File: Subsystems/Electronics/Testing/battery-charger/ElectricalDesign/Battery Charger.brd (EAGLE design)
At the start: 165 x 75 mm, 140 parts, among them J1 USB4515-GF-A_REVA, J3 10103592-0001LF, Q1 CSD16406Q3, Q2 CSD16406Q3, Q3 DMN2008LFU, Q4 DMN2008LFU, Q5 DMN2008LFU, Q6 BC817, Q7 BC817, Q8 DMN53D0L, SW6 [Override], U1 BQ24650, U2 BQ29700, U3 BQ29700, U4 BQ29700, U5 CP2102N-A02-GQFN28, U7 ESP32-S2-MINI-1

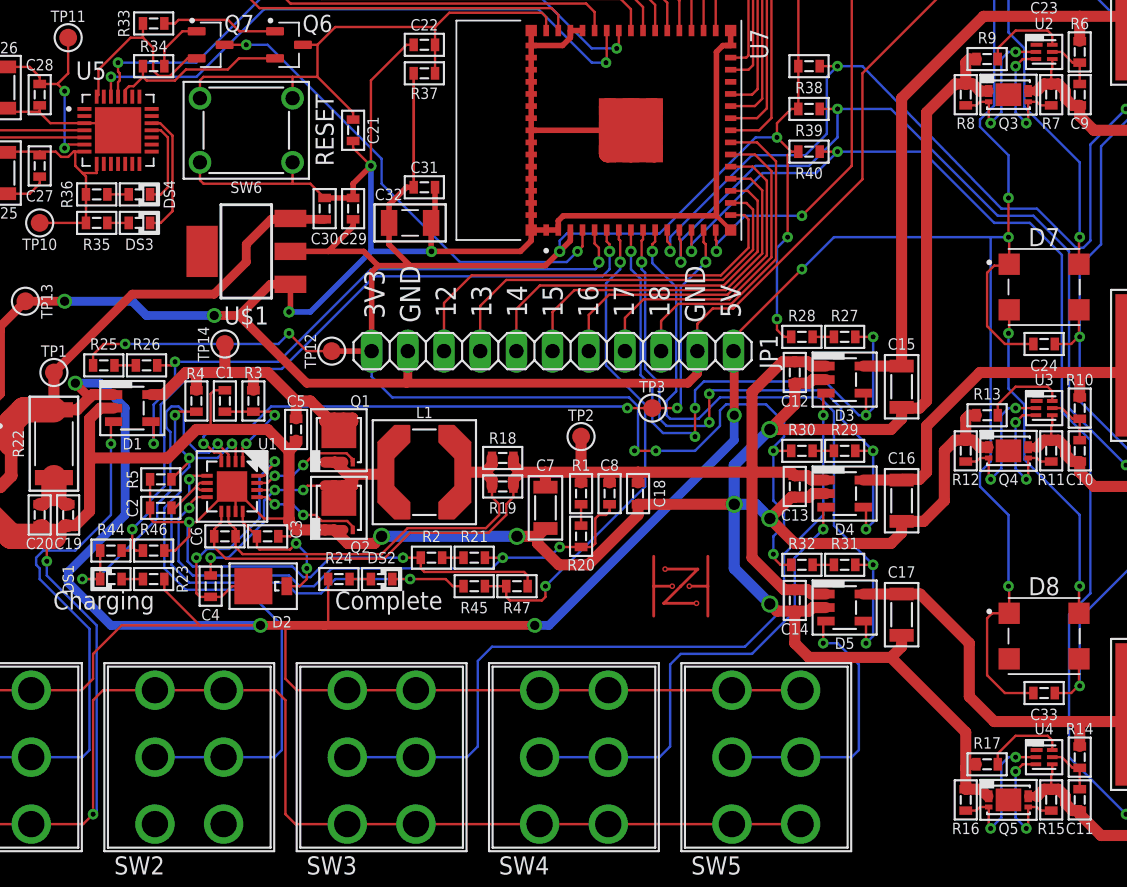
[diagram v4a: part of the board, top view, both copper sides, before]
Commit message: Removed Wire Stubs
Ran DRC a dozen times and cleaned up all the errors and wire stubs
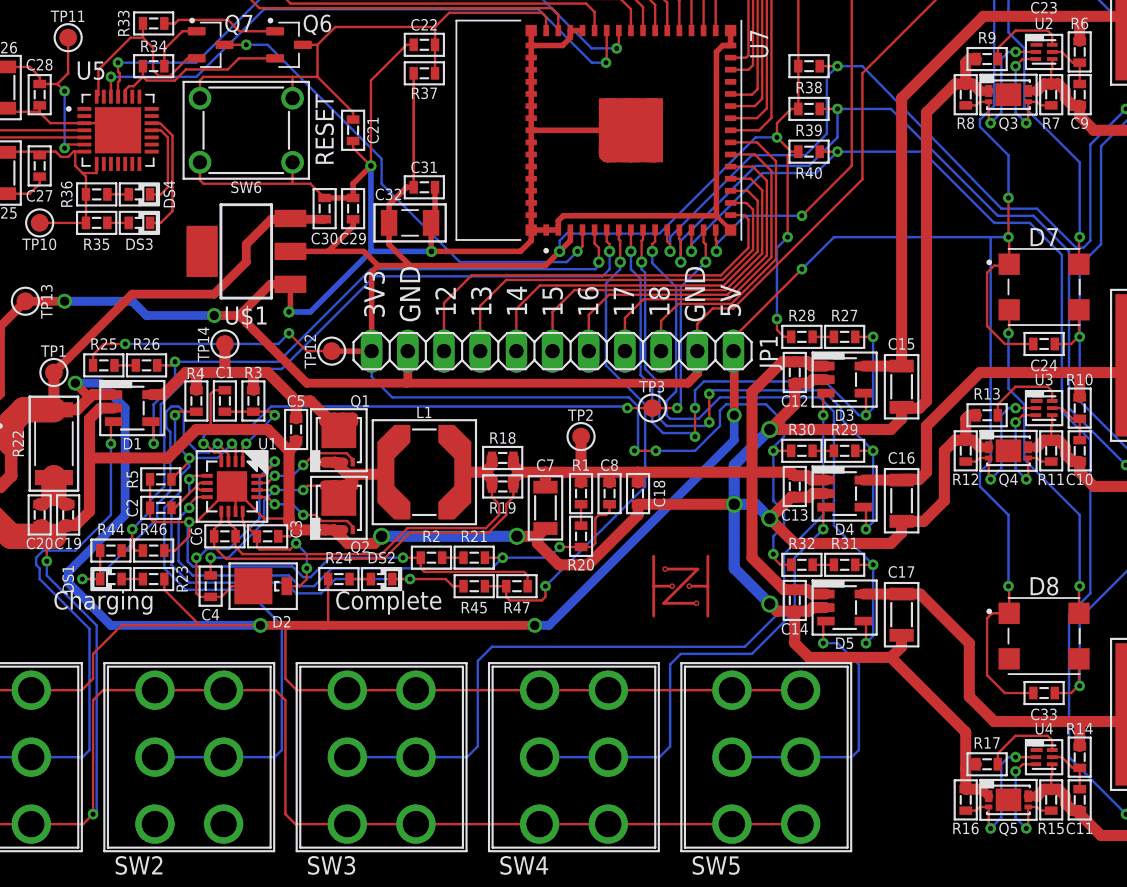
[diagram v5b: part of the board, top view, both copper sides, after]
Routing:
- net PGND: track 781.8 -> 779.6 mm
- net BQ24650_PH: track 23.8 -> 23.1 mm
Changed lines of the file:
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@@
 <wire x1="32.125" y1="26" x2="34" y2="26" width="0.78" layer="1"/>
 <wire x1="44" y1="26.5" x2="45.45" y2="26.5" width="0.78" layer="1"/>
-<wire x1="45.45" y1="26.5" x2="46" y2="27.05" width="0.78" layer="1"/>
 <wire x1="34.5" y1="26.5" x2="44" y2="26.5" width="0.78" layer="16"/>
-<wire x1="45.45" y1="26.3" x2="45.45" y2="26.5" width="0.17" layer="1"/>
 <wire x1="28.1" y1="26.5" x2="28.55" y2="26.95" width="0.17" layer="1"/>
 <wire x1="27.25" y1="26.5" x2="28.1" y2="26.5" width="0.17" layer="1"/>
 <wire x1="24" y1="30" x2="21.5" y2="27.5" width="0.17" layer="1"/>
-<wire x1="23.5" y1="36.75" x2="23.75" y2="36.75" width="0.17" layer="1"/>
 <wire x1="18.5" y1="27.5" x2="18.25" y2="27.75" width="0.17" layer="1"/>
 <wire x1="18.25" y1="27.75" x2="18.25" y2="28.5" width="0.17" layer="1"/>
@@
 <wire x1="14.75" y1="35.5" x2="14" y2="34.75" width="0.78" layer="1"/>
 <wire x1="14" y1="34.75" x2="14" y2="32" width="0.78" layer="1"/>
-<wire x1="23.5" y1="36.75" x2="22.75" y2="36.75" width="0.17" layer="1"/>
-<wire x1="22.75" y1="36.75" x2="22.5" y2="36.5" width="0.17" layer="1"/>
+<wire x1="22.5" y1="36.5" x2="22.75" y2="36.75" width="0.17" layer="1"/>
 <wire x1="22.5" y1="36.5" x2="22.5" y2="34" width="0.17" layer="1"/>
 <wire x1="52.5" y1="28.75" x2="52.5" y2="28" width="0.78" layer="1"/>
 <wire x1="46.94806875" y1="24.5" x2="45.45" y2="25.99806875" width="0.78" layer="1"/>
-<wire x1="45.45" y1="25.99806875" x2="45.45" y2="26.5" width="0.78" layer="1"/>
 <wire x1="52.5" y1="28" x2="49" y2="24.5" width="0.78" layer="1"/>
 <wire x1="49" y1="24.5" x2="46.94806875" y2="24.5" width="0.78" layer="1"/>
@@
 <wire x1="75.5" y1="58.25" x2="76" y2="58.25" width="0.78" layer="1"/>
 <wire x1="76" y1="58.25" x2="76.5" y2="57.75" width="0.78" layer="1"/>
-<wire x1="77.0526" y1="57.75" x2="76.5" y2="57.75" width="0.78" layer="1"/>
-<wire x1="77.0526" y1="57.75" x2="77.0576" y2="57.755" width="0.78" layer="1"/>
 <wire x1="71" y1="27.55" x2="72.55" y2="27.55" width="0.78" layer="1"/>
 <wire x1="74" y1="29" x2="72.55" y2="27.55" width="0.78" layer="1"/>
@@
 <wire x1="75.5" y1="33.25" x2="76" y2="33.25" width="0.78" layer="1"/>
 <wire x1="76" y1="33.25" x2="76.5" y2="32.75" width="0.78" layer="1"/>
-<wire x1="77.0526" y1="32.75" x2="76.5" y2="32.75" width="0.78" layer="1"/>
-<wire x1="77.0526" y1="32.75" x2="77.0576" y2="32.755" width="0.78" layer="1"/>
 <wire x1="75.5" y1="8.75" x2="75.5" y2="10.25" width="0.78" layer="1"/>
 <wire x1="75.5" y1="10.25" x2="75.75" y2="10.5" width="0.78" layer="1"/>
@@
 <wire x1="75.5" y1="12.75" x2="70.25" y2="18" width="0.78" layer="1"/>
 <wire x1="75.5" y1="8.75" x2="76.5626" y2="8.75" width="0.78" layer="1"/>
-<wire x1="76.5626" y1="8.75" x2="77.0576" y2="8.255" width="0.78" layer="1"/>
 <wire x1="83.45" y1="65.55" x2="83.5" y2="65.5" width="0.17" layer="1"/>
 <wire x1="83.45" y1="67.4" x2="83.45" y2="65.55" width="0.17" layer="1"/>
@@
 <wire x1="87.5" y1="24.75" x2="87.5" y2="32" width="0.17" layer="16"/>
 <wire x1="31.175" y1="26.95" x2="30.525" y2="26.95" width="0.78" layer="1"/>
-<wire x1="76.5" y1="57.75" x2="76.505" y2="57.755" width="0.16" layer="1"/>
-<wire x1="76.505" y1="57.755" x2="77.115" y2="57.755" width="0.16" layer="1"/>
-<wire x1="76.5" y1="32.75" x2="76.505" y2="32.755" width="0.16" layer="1"/>
-<wire x1="76.505" y1="32.755" x2="77.115" y2="32.755" width="0.16" layer="1"/>
-<wire x1="76.5626" y1="8.75" x2="76.62" y2="8.75" width="0.16" layer="1"/>
-<wire x1="76.62" y1="8.75" x2="77.115" y2="8.255" width="0.16" layer="1"/>
+<wire x1="76.62" y1="8.75" x2="76.5626" y2="8.75" width="0.16" layer="1"/>
 <wire x1="28.55" y1="26.95" x2="30.525" y2="26.95" width="0.78" layer="1"/>
 <contactref element="R47" pad="1"/>
@@
 <wire x1="20" y1="25.5" x2="21" y2="26.5" width="0.17" layer="1"/>
 <wire x1="21" y1="26.5" x2="21" y2="27.5" width="0.17" layer="1"/>
-<wire x1="31.825" y1="26.95" x2="31.175" y2="26.95" width="0.7" layer="1"/>
+<wire x1="31.825" y1="26.95" x2="31.175" y2="26.95" width="0.69" layer="1"/>
+<wire x1="77.115" y1="8.255" x2="76.62" y2="8.75" width="0.65" layer="1"/>
+<wire x1="45.45" y1="25.99806875" x2="45.45" y2="26.5" width="0.78" layer="1"/>
+<wire x1="45.45" y1="26.5" x2="46" y2="27.05" width="0.78" layer="1"/>
+<wire x1="22.75" y1="36.75" x2="23.5" y2="36.75" width="0.17" layer="1"/>
+<wire x1="76.5" y1="57.75" x2="77.11" y2="57.75" width="0.65" layer="1"/>
+<wire x1="77.11" y1="57.75" x2="77.115" y2="57.755" width="0.65" layer="1"/>
+<wire x1="76.5" y1="32.75" x2="77.11" y2="32.75" width="0.65" layer="1"/>
+<wire x1="77.11" y1="32.75" x2="77.115" y2="32.755" width="0.65" layer="1"/>
 </signal>
 <signal name="BQ24650_VREF">
@@
 <contactref element="Q2" pad="7"/>
 <contactref element="Q2" pad="5"/>
-<wire x1="30.475" y1="30" x2="30.525" y2="30.05" width="0.17" layer="1"/>
 <wire x1="34.6576" y1="30.8576" x2="34.8" y2="31" width="0.78" layer="1"/>
 <wire x1="32.10033125" y1="30.8576" x2="34.6576" y2="30.8576" width="0.78" layer="1"/>
@@
 <wire x1="25.75" y1="29.75" x2="27" y2="29.75" width="0.17" layer="1"/>
 <wire x1="29" y1="29.75" x2="29.3" y2="30.05" width="0.17" layer="1"/>
-<wire x1="29.3" y1="30.05" x2="30.525" y2="30.05" width="0.17" layer="1"/>
 <wire x1="27" y1="29.75" x2="29" y2="29.75" width="0.17" layer="16"/>
 <via x="22.5" y="25" extent="1-16" drill="0.35"/>
@@
 <wire x1="32.10033125" y1="30.8576" x2="32.475" y2="30.48293125" width="0.78" layer="1"/>
 <wire x1="30.525" y1="31.7" x2="31.175" y2="31.7" width="0.78" layer="1"/>
-<wire x1="31.175" y1="31.7" x2="31.7826" y2="31.7" width="0.78" layer="1"/>
 <wire x1="31.175" y1="31.7" x2="31.25793125" y2="31.7" width="0.78" layer="1"/>
 <wire x1="31.25793125" y1="31.7" x2="32.10033125" y2="30.8576" width="0.78" layer="1"/>
-<wire x1="31.175" y1="31.7" x2="31.825" y2="31.7" width="0.16" layer="1"/>
+<wire x1="31.825" y1="31.7" x2="31.175" y2="31.7" width="0.69" layer="1"/>
+<wire x1="29.3" y1="30.05" x2="30.525" y2="30.05" width="0.17" layer="1"/>
 </signal>
 <signal name="BQ24650_BTST">
@@
 <wire x1="80.495" y1="8.255" x2="80.5" y2="8.25" width="0.78" layer="1"/>
 <wire x1="80.5" y1="8.25" x2="81" y2="8.75" width="0.78" layer="1"/>
-<wire x1="79.885" y1="8.255" x2="80.495" y2="8.255" width="0.6" layer="1"/>
+<wire x1="79.885" y1="8.255" x2="80.495" y2="8.255" width="0.65" layer="1"/>
 </signal>
 <signal name="BQ297003_BAT">
@@
 <wire x1="30.5" y1="48.75" x2="28.16" y2="48.75" width="0.621" layer="1"/>
 <wire x1="28.16" y1="48.75" x2="28.099" y2="48.811" width="0.621" layer="1"/>
-<wire x1="13.8" y1="36.45" x2="14.2" y2="36.45" width="0.17" layer="1"/>
 <wire x1="28.099" y1="48.811" x2="28.038" y2="48.75" width="0.621" layer="1"/>
 <wire x1="28.038" y1="48.75" x2="26.75" y2="48.75" width="0.621" layer="1"/>
